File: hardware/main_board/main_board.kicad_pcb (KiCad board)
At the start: 2 copper layers, 96 x 72 mm, 85 parts, among them IC1 E22-900M22S, IC2 INA226AIDGST, IC3 INA226AIDGST, IC4 TPS2121RUXT, IC5 TP5000-QFN16, J1 power swith, J2 I2C External Modules, J3 Solar panel, J5 Battary over BMS, J6 USB4105-GF-A-060, U1 ESP32-C3-WROOM-02, U2 DS3231SN, U4 TPS631000DRLR, U5 PCA9536DR

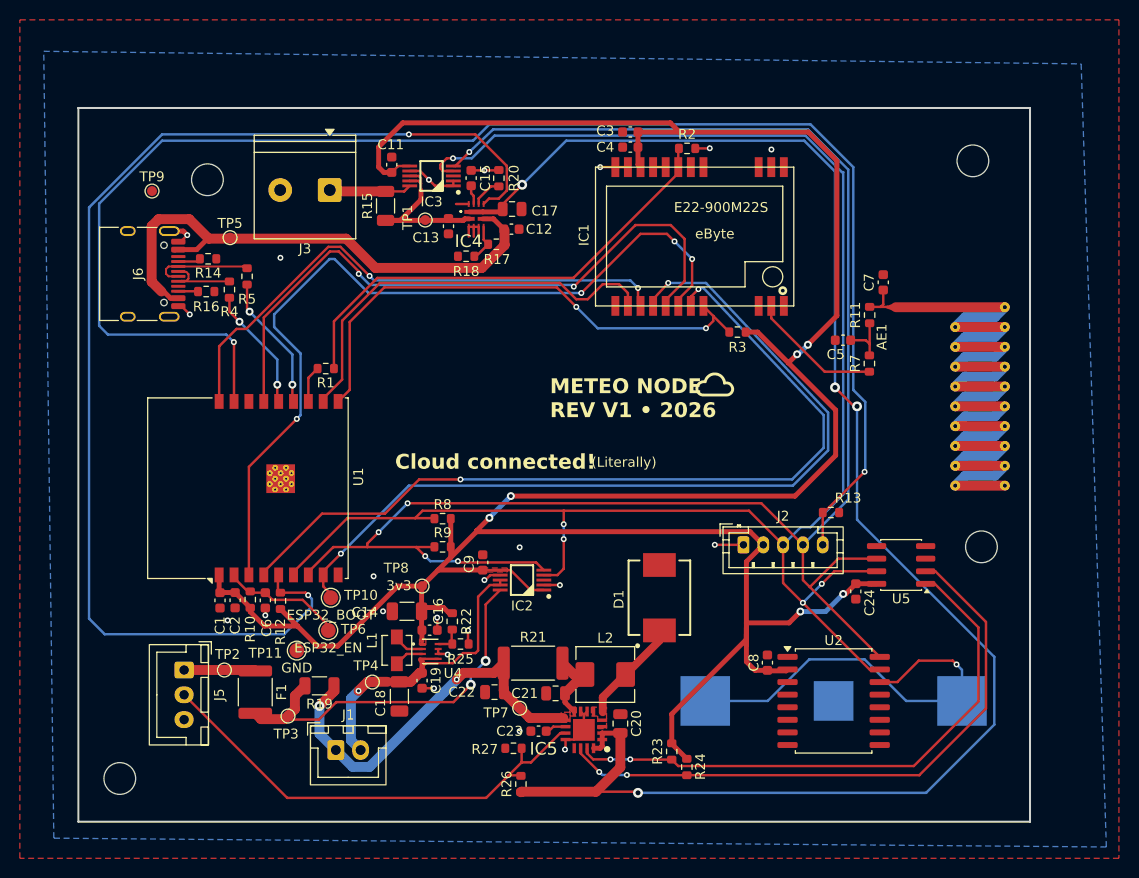
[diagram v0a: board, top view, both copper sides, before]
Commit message: hw v1 wi-fi switch
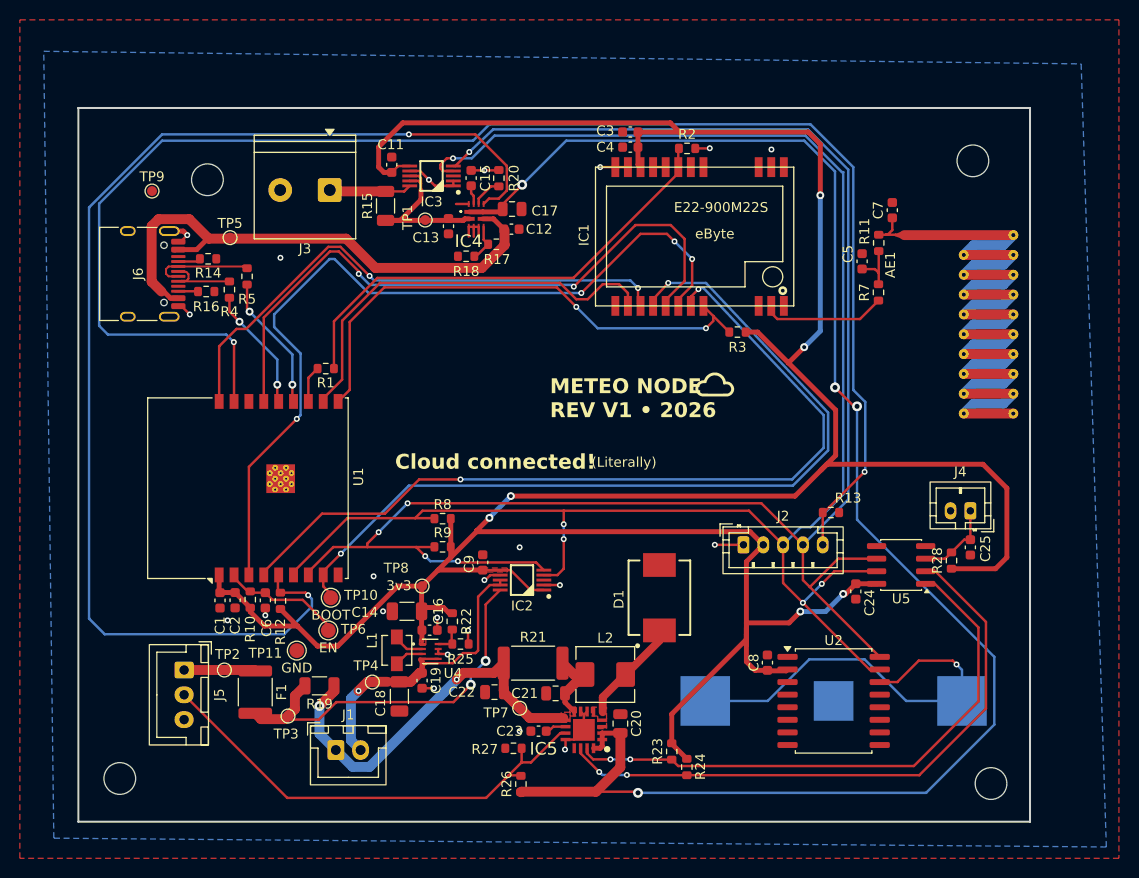
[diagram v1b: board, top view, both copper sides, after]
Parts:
- added C25: 100nF, Capacitor_SMD:C_0603_1608Metric, F.Cu at (191.8, 109.5)
- added J4: WI-FI switch, Connector_JST:JST_PH_B2B-PH-K_1x02_P2.00mm_Vertical, F.Cu at (191.8, 105.8)
- added R28: 47k, Resistor_SMD:R_0603_1608Metric, F.Cu at (189.9, 110.8)
- TP10: value ESP32_BOOT -> BOOT
- TP6: value ESP32_EN -> EN
- moved REF3 23.9 mm to (193.9, 133.3)
- moved C5 8.19 mm to (180.8, 80.6), turned to 90 degrees
- moved C7 7.33 mm to (183.9, 75.5)
- moved R11 7.33 mm to (182.5, 78.8)
- moved AE1 7.32 mm to (190.3, 87.0)
- moved R7 7.23 mm to (182.5, 83.8)
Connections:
- U5 pad 3: unconnected-(U5-IO2-Pad3) -> Net-(J4-Pin_1)
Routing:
- net +3V3: track 282.8 -> 314.3 mm
- net Net-(J4-Pin_1): track 0.00 -> 8.21 mm
- net Net-(IC1-ANT): track 14.0 -> 12.6 mm

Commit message: hw v1 cleanup
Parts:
- TP10: value BOOT -> ESP32_BOOT
- TP6: value EN -> ESP32_EN
- moved D1 10.0 mm to (164.7, 123.6)
- moved L2 4.37 mm to (158.3, 125.0), turned to 90 degrees
- moved C20 2.19 mm to (157.1, 129.3), turned to 0 degrees
- moved R25 0.13 mm to (140.2, 119.2)
- moved U4 0.13 mm to (137.2, 120.0)
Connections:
- C22 pad 1: /Power/BAT_SW -> BAT_SW
- IC2 pad 8: BAT_SYSTEM -> BAT_SW
- IC2 pad 9: BAT_SYSTEM -> BAT_SW
- IC5 pad 9: /Power/BAT_SW -> BAT_SW
- J1 pad 1: /Power/BAT_SW -> BAT_SW
- R19 pad 1: /Power/BAT_SW -> BAT_SW
- R21 pad 1: /Power/BAT_SW -> BAT_SW
- TP7 pad 1: /Power/BAT_SW -> BAT_SW
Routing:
- net BAT_SW: track 0.00 -> 63.2 mm, vias 0 -> 4
- net /Power/BAT_SW: track 39.8 -> 0.00 mm, vias 2 -> 0
- net BAT_SYSTEM: track 30.7 -> 15.7 mm
- net BAT_FUSED: track 38.3 -> 31.3 mm
- net /Power/CHARGER_IN: track 165.8 -> 161.5 mm
- net Net-(U4-LX2): track 3.19 -> 0.21 mm
- net Net-(U4-LX1): track 2.98 -> 0.00 mm
- net GND: track 41.7 -> 43.0 mm, vias 22 -> 26
- net +3V3: track 314.3 -> 315.2 mm
- net /main_board/WAKE_IRQ: track 154.2 -> 155.0 mm
- net Net-(IC5-VS): track 7.76 -> 8.48 mm
- added copper zone on F.Cu, net Net-(U4-LX1)
- added copper zone on F.Cu, net Net-(U4-LX2)

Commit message: hw v1 cleanup
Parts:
- moved D1 8.49 mm to (162.1, 131.7), turned to 0 degrees
- moved R23 7.87 mm to (169.5, 130.9)
- moved R24 7.77 mm to (170.9, 131.7)
- moved C20 2.06 mm to (156.4, 131.3), turned to -90 degrees
- moved TP11 0.20 mm to (123.6, 120.0)
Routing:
- net +3V3: track 315.2 -> 309.1 mm
- net /Power/CHARGER_IN: track 161.5 -> 156.5 mm
- net STDBY_STATUS: track 62.1 -> 62.9 mm
- net CHRG_STATUS: track 58.2 -> 58.7 mm
- net GND: track 43.0 -> 42.8 mm, vias 26 -> 30
- added copper zone on F.Cu, net /Power/CHARGER_IN

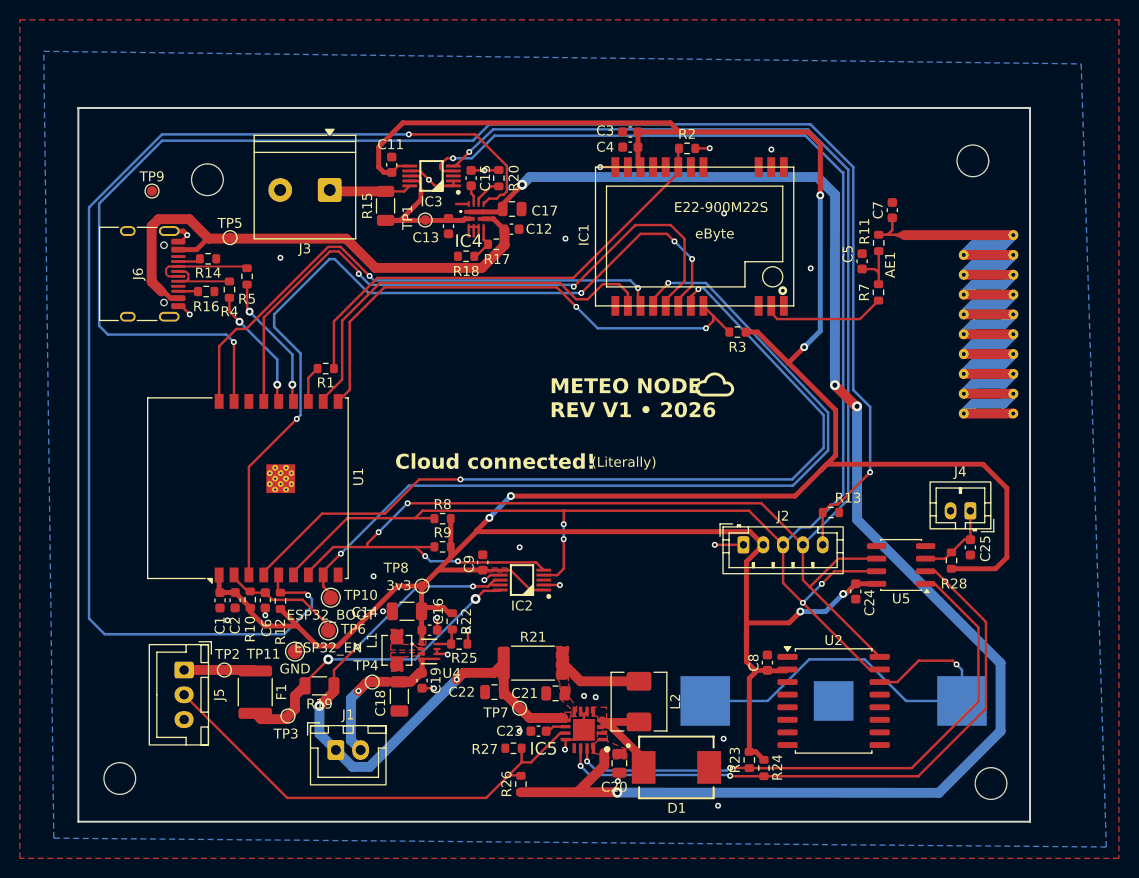
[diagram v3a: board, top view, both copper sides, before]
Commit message: hw v1 battery selection
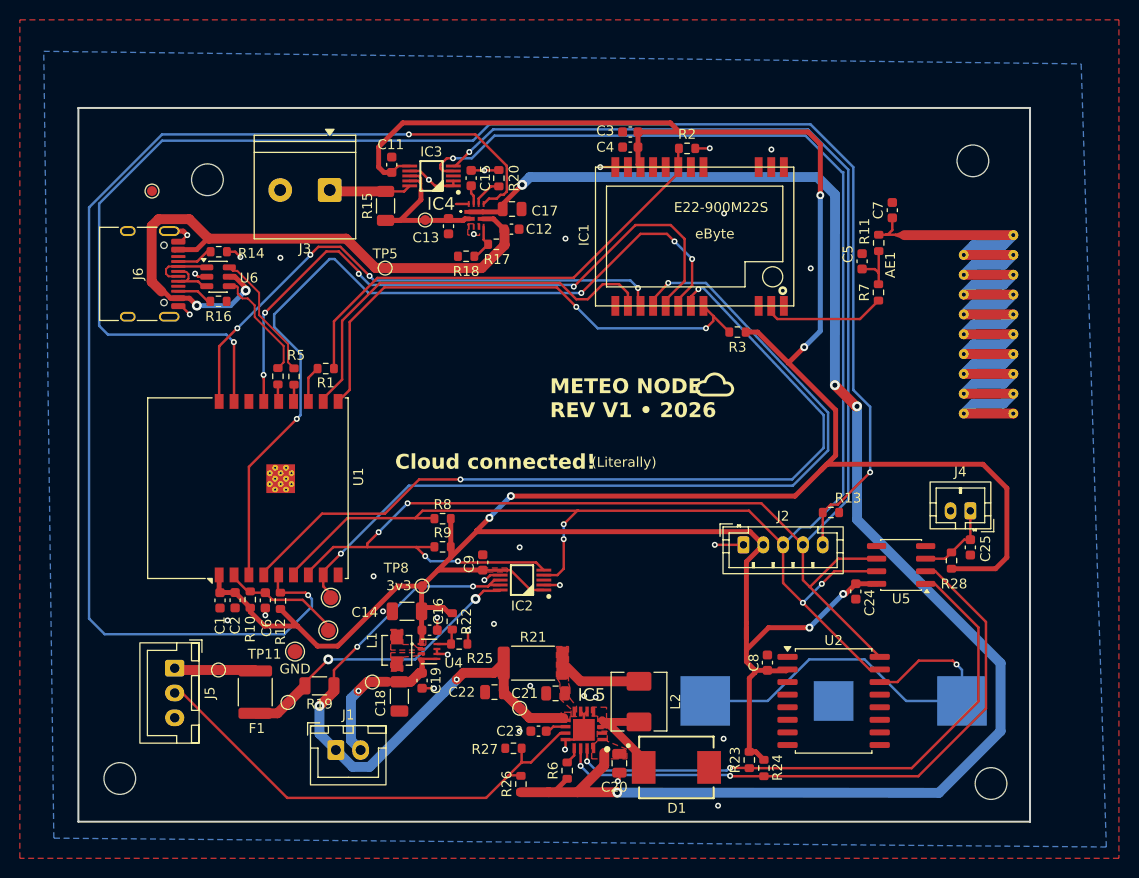
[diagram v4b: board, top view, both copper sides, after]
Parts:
- added R6: 0R, Resistor_SMD:R_0603_1608Metric, F.Cu at (151.1, 132.0)
- added U6: USBLC6-2SC6, Package_TO_SOT_SMD:SOT-23-6, F.Cu at (115.9, 82.2)
- moved TP5 15.9 mm to (132.7, 81.3)
- moved R5 11.2 mm to (123.5, 92.2)
- moved R4 10.0 mm to (121.9, 92.2)
- moved R16 1.59 mm to (115.9, 84.7)
- moved TP3 1.37 mm to (122.9, 125.1)
- moved R14 1.29 mm to (116.0, 79.7)
- moved J5 0.97 mm to (111.5, 121.7)
- moved TP2 0.59 mm to (115.9, 121.8)
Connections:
- IC5 pad 13: unconnected-(IC5-CS-Pad13) -> Net-(IC5-CS)
- J6 pad A6: USB_D+ -> Net-(J6-D+-PadA6)
- J6 pad A7: USB_D- -> Net-(J6-D--PadA7)
- J6 pad B6: USB_D+ -> Net-(J6-D+-PadA6)
- J6 pad B7: USB_D- -> Net-(J6-D--PadA7)
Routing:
- net Net-(U1-IO18): track 13.7 -> 1.71 mm, vias 2 -> 0
- net Net-(U1-IO19): track 12.5 -> 1.75 mm, vias 2 -> 0
- net /Power/USB_5V: track 56.1 -> 66.2 mm, vias 0 -> 2
- net Net-(J6-D+-PadA6): track 0.00 -> 5.93 mm
- net Net-(J6-D--PadA7): track 0.00 -> 5.35 mm
- net USB_D+: track 7.78 -> 11.5 mm
- net USB_D-: track 9.81 -> 13.2 mm
- net /Power/CHARGER_IN: track 156.5 -> 159.0 mm
- net Net-(IC5-CS): track 0.00 -> 1.73 mm
- net Net-(J6-CC2): track 2.36 -> 4.01 mm
- net Net-(J6-CC1): track 2.66 -> 4.03 mm
- net BAT_FUSED: track 31.3 -> 30.0 mm
- net GND: track 42.8 -> 41.7 mm, vias 30 -> 35
- net /Power/NTC_SENSE: track 48.2 -> 49.2 mm
- net /Power/BAT_RAW: track 7.22 -> 8.24 mm
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
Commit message: hw v1 clean up
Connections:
- net Net-(J4-Pin_1) renamed /main_board/WIFI_SW

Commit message: software
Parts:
- added F2: 0ZCK0075FF2E, Fuse:Fuse_0805_2012Metric, F.Cu at (115.1, 77.9)
- added F3: 0ZCH0075AF2E, Fuse:Fuse_1210_3225Metric, F.Cu at (130.1, 72.6)
- added R29: 0R, Resistor_SMD:R_0603_1608Metric, F.Cu at (138.2, 111.7)
- R15: value 100mR -> 20mR
- moved REF1 8.59 mm to (106.9, 69.0)
- moved TP9 4.16 mm to (113.3, 72.6)
- moved TP8 3.41 mm to (139.8, 114.0)
- moved REF2 2.16 mm to (193.4, 68.8)
- moved R1 1.85 mm to (125.1, 92.2), turned to -90 degrees
- moved J3 1.59 mm to (125.6, 73.4)
- moved REF4 1.06 mm to (106.9, 133.2)
- moved REF3 0.47 mm to (193.4, 133.5)
- moved R15 0.19 mm to (133.0, 75.1)
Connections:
- C14 pad 1: +3V3 -> Net-(U4-VOUT)
- C16 pad 1: +3V3 -> Net-(U4-VOUT)
- J3 pad 1: SOLAR+ -> Net-(J3-Pin_1)
- J6 pad A4: /Power/USB_5V -> Net-(F2-Pad1)
- J6 pad A9: /Power/USB_5V -> Net-(F2-Pad1)
- J6 pad B4: /Power/USB_5V -> Net-(F2-Pad1)
- J6 pad B9: /Power/USB_5V -> Net-(F2-Pad1)
- R22 pad 1: +3V3 -> Net-(U4-VOUT)
- TP8 pad 1: +3V3 -> Net-(U4-VOUT)
- U4 pad 1: +3V3 -> Net-(U4-VOUT)
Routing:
- net CHARGE_SOURCE_STATUS_OUT: track 123.8 -> 83.3 mm
- net /Power/USB_5V: track 66.2 -> 45.0 mm
- net Net-(F2-Pad1): track 0.00 -> 18.7 mm
- net Net-(U4-VOUT): track 0.00 -> 12.8 mm
- net +3V3: track 309.1 -> 299.7 mm
- net /main_board/SPI_MOSI: track 84.3 -> 76.1 mm
- net Net-(J3-Pin_1): track 0.00 -> 5.48 mm
- net SOLAR+: track 8.69 -> 5.71 mm
- net Net-(U1-IO21/TXD): track 3.70 -> 1.75 mm
- net /main_board/WAKE_IRQ: track 155.0 -> 153.1 mm
- net /main_board/LORA_RXEN: track 48.2 -> 49.2 mm
- net /main_board/SPI_MISO: track 66.2 -> 65.8 mm, vias 4 -> 2
- net /main_board/LORA_BUSY: track 55.6 -> 55.4 mm, vias 4 -> 2
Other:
- board size 96 x 72 mm -> 94 x 72 mm
